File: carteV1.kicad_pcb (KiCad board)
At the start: 2 copper layers, 62 parts, among them CON1 USB-MINI-B, J12 FILTER_IOUT_DUT2, J7 CRYSTAL OUTDUT2, P1 CONN_2X2, P2 CONN_2X2, P3 CONN_2, P4 CONN_2X2, P5 CONN_8, T8 T1-1T, U1 AD9954, U2 LM1117MP-1.8, U3 LM1117MP-1.8, U4 LM1117MP-3.3, U5 MCP2210-SO, X1 25mhz, X2 12mhz

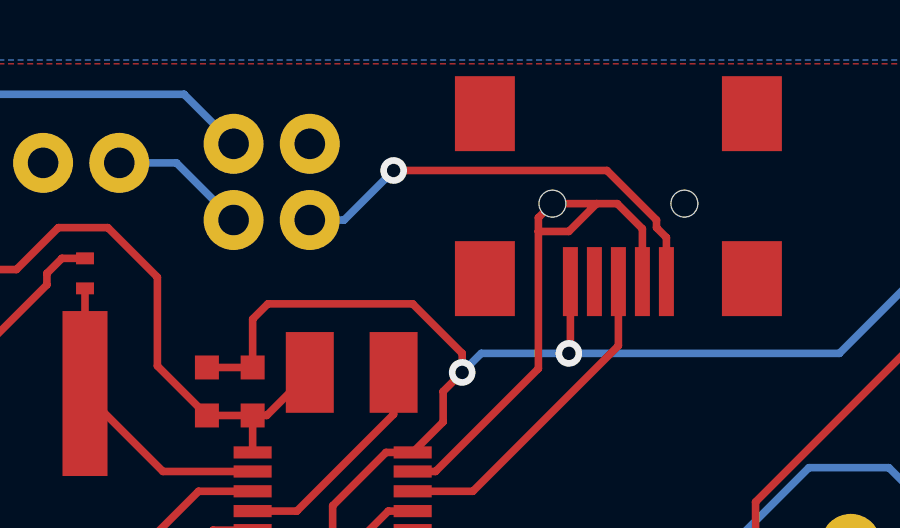
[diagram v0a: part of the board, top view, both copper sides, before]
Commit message: Final version without the I/O update pin connected
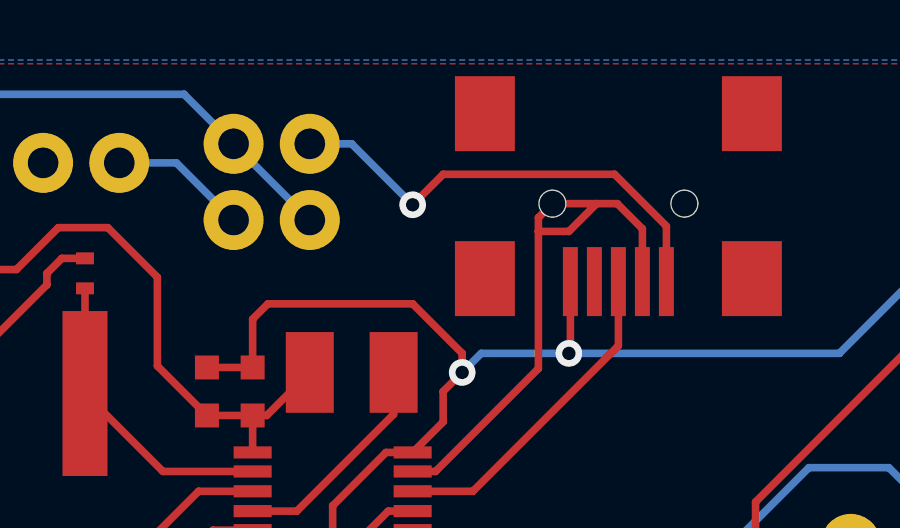
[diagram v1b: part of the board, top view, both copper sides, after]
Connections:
- CON1 pad 1: N-0000014 -> N-0000026
- P2 pad 3: N-0000014 -> 5V
- P2 pad 4: (no net) -> N-0000026
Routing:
- net N-0000026: track 0.00 -> 15.7 mm, vias 0 -> 1
- net N-0000014: track 15.1 -> 0.00 mm, vias 1 -> 0
- net 5V: track 81.0 -> 84.6 mm
